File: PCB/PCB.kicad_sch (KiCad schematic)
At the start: 16 parts, among them J1 Screw_Terminal_01x02, J2 Screw_Terminal_01x02, U1 MPU-6050, U2 DRV8833PWP, U3 ESP32-S3-MINI-1

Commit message: PCB work, finished schematic Rev A
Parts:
- added C10, C11, C12, C13, C14, C9: 10uF, symbol Device:C
- added C15: 1uF, symbol Device:C
- added C16, C7: 1uF 50V, symbol Device:C
- added C8: 10uF 25V, symbol Device:C
- added D1: 1N5819, Diode_THT:D_DO-41_SOD81_P10.16mm_Horizontal, symbol Diode:1N5819
- added D2: LED, symbol Device:LED
- added J3: USB_C_Receptacle_USB2.0_14P, symbol Connector:USB_C_Receptacle_USB2.0_14P
- added R10, R6, R7, R8: 5.1K, symbol Device:R
- added R9: 100K, symbol Device:R
- added SW1, SW2: SW_Push, symbol Switch:SW_Push
- added U4: AP2112K-3.3, Package_TO_SOT_SMD:SOT-23-5, symbol Regulator_Linear:AP2112K-3.3
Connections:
- net +3.3V: now also U3.3 (3V3), C10.1, C11.1, C12.1, C13.1, C14.1, C15.1, R10.1, R6.1, U4.5 (VOUT)
- net +5V: now also C8.1, C9.1, D1.1 (K), R9.2, U4.1 (VIN)
- net AIN1: now also U3.21 (IO17)
- net AIN2: now also U3.9 (IO5)
- net BIN1: now also U3.22 (IO18)
- net BIN2: now also U3.10 (IO6)
- net GND: now also U3.1 (GND), U3.2 (GND), U3.42 (GND), U3.43 (GND), U3.46 (GND), U3.47 (GND), U3.48 (GND), U3.49 (GND), U3.50 (GND), U3.51 (GND), U3.52 (GND), U3.53 (GND), U3.54 (GND), U3.55 (GND), U3.56 (GND), U3.57 (GND), U3.58 (GND), U3.59 (GND), U3.60 (GND), U3.61 (GND), U3.62 (GND), U3.63 (GND), U3.64 (GND), U3.65 (GND), C10.2, C11.2, C12.2, C13.2, C14.2, C15.2, C16.2, C7.2, C8.2, C9.2, D2.1 (K), J3.A1 (GND), J3.A12 (GND), J3.B1 (GND), J3.B12 (GND), J3.S1 (SHIELD), R7.2, R8.2, SW1.2, SW2.1, U4.2 (GND)
- net SCL: now also U3.8 (IO4)
- net IO7: now reaches U3.11 (IO7)
- net IO8: now reaches U3.12 (IO8)
- net IO9: now reaches U3.13 (IO9)
- net IO10: now reaches U3.14 (IO10)
- net IO11: now reaches U3.15 (IO11)
- net IO12: now reaches U3.16 (IO12)
- net IO13: now reaches U3.17 (IO13)
- net IO14: now reaches U3.18 (IO14)
- net IO15: now reaches U3.19 (IO15)
- net IO16: now reaches U3.20 (IO16)
- net D-: now reaches U3.23 (IO19)
- net D-: now also J3.A7 (D-), J3.B7 (D-)
- net D+: now reaches U3.24 (IO20)
- net D+: now also J3.A6 (D+), J3.B6 (D+)
- net IO21: now reaches U3.25 (IO21)
- net IO26: now reaches U3.26 (IO26)
- net IO47: now reaches U3.27 (IO47)
- net IO33: now reaches U3.28 (IO33)
- net IO34: now reaches U3.29 (IO34)
- net IO48: now reaches U3.30 (IO48)
- net IO35: now reaches U3.31 (IO35)
- net IO36: now reaches U3.32 (IO36)
- net IO37: now reaches U3.33 (IO37)
- net IO38: now reaches U3.34 (IO38)
- net IO39: now reaches U3.35 (IO39)
- net IO40: now reaches U3.36 (IO40)
- net IO41: now reaches U3.37 (IO41)
- net IO42: now reaches U3.38 (IO42)
- net TXD0: now reaches U3.39 (TXD0)
- net BOOT0: now reaches U3.4 (IO0)
- net BOOT0: now also C16.1, SW2.2
- net RXD0: now reaches U3.40 (RXD0)
- net IO45: now reaches U3.41 (IO45)
- net IO46: now reaches U3.44 (IO46)
- net RESET: now reaches U3.45 (EN)
- net RESET: now also C7.1, R6.2, SW1.1
- net IO1: now reaches U3.5 (IO1)
- net IO2: now reaches U3.6 (IO2)
- net IO3: now reaches U3.7 (IO3)
- net INT: now reaches U1.12 (INT)
- net XDA: now reaches U1.6 (AUX_DA)
- net XCL: now reaches U1.7 (AUX_CL)
- net FAULT: now reaches U2.8 (~{FAULT})
- new net: D1.2 (A), J3.A4 (VBUS), J3.A9 (VBUS), J3.B4 (VBUS), J3.B9 (VBUS)
- new net: D2.2 (A), R10.2
- new net: J3.A5 (CC1), R8.1
- new net: J3.B5 (CC2), R7.1
- new net: R9.1, U4.3 (EN)
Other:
- note added: "ESP32"
- moved on the sheet: U3

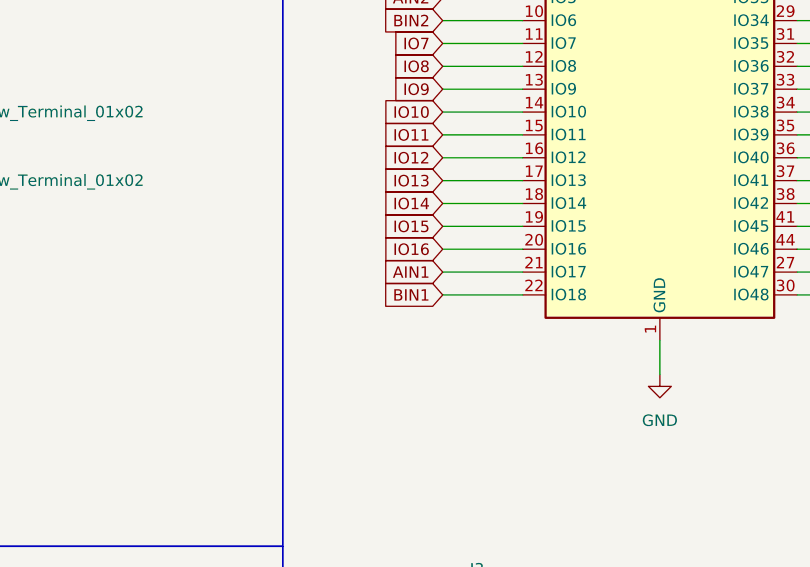
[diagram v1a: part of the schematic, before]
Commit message: Added footprints and nets to PCB file, set up design rules
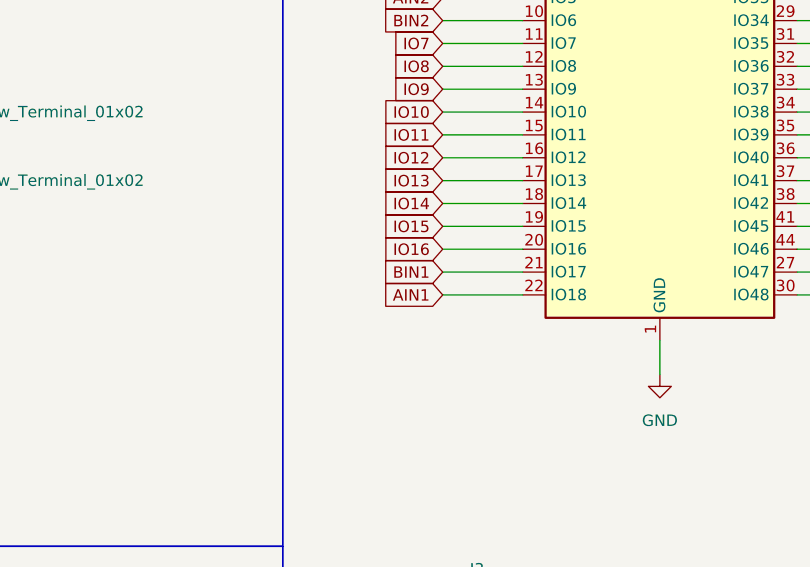
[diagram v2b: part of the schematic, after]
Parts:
- C1, C10, C11, C12, C13, C14, C15, C16, C2, C3, C4, C5, C6, C7, C8, C9: footprint (none) -> Capacitor_SMD:C_0805_2012Metric
- D2: footprint (none) -> LED_SMD:LED_0805_2012Metric
- J1, J2: footprint (none) -> Connector_Phoenix_GMSTB:PhoenixContact_GMSTBA_2,5_2-G_1x02_P7.50mm_Horizontal
- R1, R10, R2, R3, R4, R5, R6, R7, R8, R9: footprint (none) -> Resistor_SMD:R_0805_2012Metric
- SW1, SW2: footprint (none) -> Button_Switch_SMD:SW_SPST_EVPBF
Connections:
- net AIN1: now also U3.22 (IO18); no longer U3.21 (IO17)
- net BIN1: now also U3.21 (IO17); no longer U3.22 (IO18)
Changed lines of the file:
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@@
 	(wire
 		(pts
-			(xy 163.83 85.09) (xy 172.72 85.09)
-		)
-		(stroke
-			(width 0)
-			(type default)
-		)
-	)
-	(wire
-		(pts
 			(xy 203.2 57.15) (xy 210.82 57.15)
 		)
@@
 	(wire
 		(pts
-			(xy 163.83 87.63) (xy 172.72 87.63)
-		)
-		(stroke
-			(width 0)
-			(type default)
-		)
-	)
-	(wire
-		(pts
 			(xy 163.83 72.39) (xy 172.72 72.39)
 		)
@@
 	(wire
 		(pts
+			(xy 163.83 85.09) (xy 172.72 85.09)
+		)
+		(stroke
+			(width 0)
+			(type default)
+		)
+	)
+	(wire
+		(pts
 			(xy 163.83 46.99) (xy 172.72 46.99)
 		)
@@
 	(wire
 		(pts
+			(xy 163.83 87.63) (xy 172.72 87.63)
+		)
+		(stroke
+			(width 0)
+			(type default)
+		)
+	)
+	(wire
+		(pts
 			(xy 120.65 187.96) (xy 120.65 165.1)
 		)
@@
 	(global_label "BIN1"
 		(shape input)
-		(at 163.83 87.63 180)
+		(at 163.83 85.09 180)
 		(fields_autoplaced yes)
 		(effects
@@
 		)
 		(property "Intersheetrefs" "${INTERSHEET_REFS}"
-			(at 156.43 87.63 0)
+			(at 156.43 85.09 0)
 			(effects
 				(font
@@
 	(global_label "AIN1"
 		(shape input)
-		(at 163.83 85.09 180)
+		(at 163.83 87.63 180)
 		(fields_autoplaced yes)
 		(effects
@@
 		)
 		(property "Intersheetrefs" "${INTERSHEET_REFS}"
-			(at 156.6114 85.09 0)
+			(at 156.6114 87.63 0)
 			(effects
 				(font
@@
 			)
 		)
-		(property "Footprint" ""
+		(property "Footprint" "Resistor_SMD:R_0805_2012Metric"
 			(at 23.622 138.43 90)
 			(effects
@@
 			)
 		)
-		(property "Footprint" ""
+		(property "Footprint" "Resistor_SMD:R_0805_2012Metric"
 			(at 33.782 66.04 90)
 			(effects
@@
 			)
 		)
-		(property "Footprint" ""
+		(property "Footprint" "Connector_Phoenix_GMSTB:PhoenixContact_GMSTBA_2,5_2-G_1x02_P7.50mm_Horizontal"
 			(at 107.95 72.39 0)
 			(effects
@@
 			)
 		)
-		(property "Footprint" ""
+		(property "Footprint" "Capacitor_SMD:C_0805_2012Metric"
 			(at 352.7552 99.06 0)
 			(effects
@@
 			)
 		)
-		(property "Footprint" ""
+		(property "Footprint" "Capacitor_SMD:C_0805_2012Metric"
 			(at 122.8852 137.16 0)
 			(effects
@@
 			)
 		)
-		(property "Footprint" ""
+		(property "Footprint" "LED_SMD:LED_0805_2012Metric"
 			(at 382.27 95.25 0)
 			(effects
@@
 			)
 		)
-		(property "Footprint" ""
+		(property "Footprint" "Resistor_SMD:R_0805_2012Metric"
 			(at 268.732 135.89 90)
 			(effects
@@
 			)
 		)
-		(property "Footprint" ""
+		(property "Footprint" "Resistor_SMD:R_0805_2012Metric"
 			(at 46.482 167.64 90)
 			(effects
@@
 			)
 		)
-		(property "Footprint" ""
+		(property "Footprint" "Resistor_SMD:R_0805_2012Metric"
 			(at 210.312 139.7 90)
 			(effects
@@
 			)
 		)
-		(property "Footprint" ""
+		(property "Footprint" "Capacitor_SMD:C_0805_2012Metric"
 			(at 224.4852 143.51 0)
 			(effects
@@
 			)
 		)
-		(property "Footprint" ""
+		(property "Footprint" "Resistor_SMD:R_0805_2012Metric"
 			(at 200.152 139.7 90)
 			(effects
@@
 			)
 		)
-		(property "Footprint" ""
+		(property "Footprint" "Capacitor_SMD:C_0805_2012Metric"
 			(at 74.93 139.3952 0)
 			(effects
@@
 			)
 		)
-		(property "Footprint" ""
+		(property "Footprint" "Resistor_SMD:R_0805_2012Metric"
 			(at 43.942 66.04 90)
 			(effects
@@
 			)
 		)
-		(property "Footprint" ""
+		(property "Footprint" "Capacitor_SMD:C_0805_2012Metric"
 			(at 324.8152 99.06 0)
 			(effects
@@
 			)
 		)
-		(property "Footprint" ""
+		(property "Footprint" "Button_Switch_SMD:SW_SPST_EVPBF"
 			(at 350.52 137.16 0)
 			(effects
@@
 			)
 		)
-		(property "Footprint" ""
+		(property "Footprint" "Resistor_SMD:R_0805_2012Metric"
 			(at 374.65 90.678 90)
 			(effects
@@
 			)
 		)
-		(property "Footprint" ""
+		(property "Footprint" "Capacitor_SMD:C_0805_2012Metric"
 			(at 338.7852 99.06 0)
 			(effects
@@
 			)
 		)
-		(property "Footprint" ""
+		(property "Footprint" "Capacitor_SMD:C_0805_2012Metric"
 			(at 53.0352 53.34 0)
 			(effects
@@
 			)
 		)
-		(property "Footprint" ""
+		(property "Footprint" "Capacitor_SMD:C_0805_2012Metric"
 			(at 80.01 188.9252 0)
 			(effects
@@
 			)
 		)
-		(property "Footprint" ""
+		(property "Footprint" "Connector_Phoenix_GMSTB:PhoenixContact_GMSTBA_2,5_2-G_1x02_P7.50mm_Horizontal"
 			(at 107.95 64.77 0)
 			(effects
@@
 			)
 		)
-		(property "Footprint" ""
+		(property "Footprint" "Capacitor_SMD:C_0805_2012Metric"
 			(at 366.7252 99.06 0)
 			(effects
@@
 			)
 		)
-		(property "Footprint" ""
+		(property "Footprint" "Capacitor_SMD:C_0805_2012Metric"
 			(at 287.9852 156.21 0)
 			(effects
@@
 			)
 		)
-		(property "Footprint" ""
+		(property "Footprint" "Button_Switch_SMD:SW_SPST_EVPBF"
 			(at 275.59 152.4 0)
 			(effects
@@
 			)
 		)
-		(property "Footprint" ""
+		(property "Footprint" "Resistor_SMD:R_0805_2012Metric"
 			(at 267.97 94.742 90)
 			(effects
@@
 			)
 		)
-		(property "Footprint" ""
+		(property "Footprint" "Capacitor_SMD:C_0805_2012Metric"
 			(at 254.9652 101.6 0)
 			(effects
@@
 			)
 		)
-		(property "Footprint" ""
+		(property "Footprint" "Capacitor_SMD:C_0805_2012Metric"
 			(at 131.7752 171.45 0)
 			(effects
@@
 			)
 		)
-		(property "Footprint" ""
+		(property "Footprint" "Resistor_SMD:R_0805_2012Metric"
 			(at 46.482 138.43 90)
 			(effects
@@
 			)
 		)
-		(property "Footprint" ""
+		(property "Footprint" "Capacitor_SMD:C_0805_2012Metric"
 			(at 359.1052 154.94 0)
 			(effects
@@
 			)
 		)
-		(property "Footprint" ""
+		(property "Footprint" "Capacitor_SMD:C_0805_2012Metric"
 			(at 310.8452 99.06 0)
 			(effects
@@
 			)
 		)
-		(property "Footprint" ""
+		(property "Footprint" "Capacitor_SMD:C_0805_2012Metric"
 			(at 296.8752 99.06 0)
 			(effects
@@
 			)
 		)
-		(property "Footprint" ""
+		(property "Footprint" "Capacitor_SMD:C_0805_2012Metric"
 			(at 86.36 39.0652 0)
 			(effects

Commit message: PCB Progress
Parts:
- removed J3: USB_C_Receptacle_USB2.0_14P, symbol Connector:USB_C_Receptacle_USB2.0_14P
- added J3: USB_C_Receptacle_USB2.0_16P, Connector_USB:USB_C_Receptacle_G-Switch_GT-USB-7010ASV, symbol Connector:USB_C_Receptacle_USB2.0_16P
- J1: footprint Connector_Phoenix_GMSTB:PhoenixContact_GMSTBA_2,5_2-G_1x02_P7.50mm_Horizontal -> Connector_PinSocket_2.54mm:PinSocket_1x02_P2.54mm_Vertical
- J2: footprint Connector_Phoenix_GMSTB:PhoenixContact_GMSTBA_2,5_2-G_1x02_P7.50mm_Horizontal -> Connector_PinHeader_2.54mm:PinHeader_1x02_P2.54mm_Vertical
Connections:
- net D+: now also J3.A6 (D+), J3.B6 (D+)
- net D-: now also J3.A7 (D-), J3.B7 (D-)
- net GND: now also J3.A1 (GND), J3.A12 (GND), J3.B1 (GND), J3.B12 (GND), J3.S1 (SHIELD)
- net at D1.2 (A): now also J3.A4 (VBUS), J3.A9 (VBUS), J3.B4 (VBUS), J3.B9 (VBUS)
- net at R8.1: now also J3.A5 (CC1)
- net at R7.1: now also J3.B5 (CC2)
- new net SBU1: J3.A8 (SBU1)
- new net SBU2: J3.B8 (SBU2)
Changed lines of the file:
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@@
 		)
 	)
+	(global_label "SBU2"
+		(shape input)
+		(at 182.88 156.21 0)
+		(fields_autoplaced yes)
+		(effects
+			(font
+				(size 1.27 1.27)
+			)
+			(justify left)
+		)
+		(property "Intersheetrefs" "${INTERSHEET_REFS}"
+			(at 190.8847 156.21 0)
+			(effects
+				(font
+					(size 1.27 1.27)
+				)
+				(justify left)
+				(hide yes)
+			)
+		)
+	)
 	(global_label "IO46"
 		(shape input)
@@
 		)
 	)
+	(global_label "SBU1"
+		(shape input)
+		(at 182.88 153.67 0)
+		(fields_autoplaced yes)
+		(effects
+			(font
+				(size 1.27 1.27)
+			)
+			(justify left)
+		)
+		(property "Intersheetrefs" "${INTERSHEET_REFS}"
+			(at 190.8847 153.67 0)
+			(effects
+				(font
+					(size 1.27 1.27)
+				)
+				(justify left)
+				(hide yes)
+			)
+		)
+	)
 	(global_label "IO33"
 		(shape input)
@@
 			)
 		)
-		(property "Footprint" "Connector_Phoenix_GMSTB:PhoenixContact_GMSTBA_2,5_2-G_1x02_P7.50mm_Horizontal"
+		(property "Footprint" "Connector_PinHeader_2.54mm:PinHeader_1x02_P2.54mm_Vertical"
 			(at 107.95 72.39 0)
 			(effects
@@
 			)
 		)
-		(property "Footprint" "Connector_Phoenix_GMSTB:PhoenixContact_GMSTBA_2,5_2-G_1x02_P7.50mm_Horizontal"
+		(property "Footprint" "Connector_PinSocket_2.54mm:PinSocket_1x02_P2.54mm_Vertical"
 			(at 107.95 64.77 0)
 			(effects
@@
 	)
 	(symbol
+		(lib_id "Connector:USB_C_Receptacle_USB2.0_16P")
+		(at 167.64 140.97 0)
+		(unit 1)
+		(exclude_from_sim no)
+		(in_bom yes)
+		(on_board yes)
+		(dnp no)
+		(fields_autoplaced yes)
+		(property "Reference" "J3"
+			(at 167.64 118.11 0)
+			(effects
+				(font
+					(size 1.27 1.27)
+				)
+			)
+		)
+		(property "Value" "USB_C_Receptacle_USB2.0_16P"
+			(at 167.64 120.65 0)
+			(effects
+				(font
+					(size 1.27 1.27)
+				)
+			)
+		)
+		(property "Footprint" "Connector_USB:USB_C_Receptacle_G-Switch_GT-USB-7010ASV"
+			(at 171.45 140.97 0)
+			(effects
+				(font
+					(size 1.27 1.27)
+				)
+				(hide yes)
+			)
+		)
+		(property "Datasheet" "https://www.usb.org/sites/default/files/documents/usb_type-c.zip"
+			(at 171.45 140.97 0)
+			(effects
+				(font
+					(size 1.27 1.27)
+				)
+				(hide yes)
+			)
+		)
+		(property "Description" "USB 2.0-only 16P Type-C Receptacle connector"
+			(at 167.64 140.97 0)
+			(effects
+				(font
+					(size 1.27 1.27)
+				)
+				(hide yes)
+			)
+		)
+		(pin "A1"
+		)
+		(pin "B4"
+		)
+		(pin "A8"
+		)
+		(pin "A4"
+		)
+		(pin "A9"
+		)
+		(pin "A12"
+		)
+		(pin "B6"
+		)
+		(pin "B7"
+		)
+		(pin "B5"
+		)
+		(pin "A6"
+		)
+		(pin "S1"
+		)
+		(pin "A5"
+		)
+		(pin "A7"
+		)
+		(pin "B1"
+		)
+		(pin "B12"
+		)
+		(pin "B8"
+		)
+		(pin "B9"
+		)
+		(instances
+			(project ""
+				(path "/1d0c519c-16f4-4a16-b94e-0bddce7294e9"
+					(reference "J3")
+					(unit 1)
+				)
+			)
+		)
+	)
+	(symbol
 		(lib_id "Switch:SW_Push")
 		(at 270.51 152.4 270)
@@
 					(unit 1)
 				)
-			)
-		)
-	)
-	(symbol
-		(lib_id "Connector:USB_C_Receptacle_USB2.0_14P")
-		(at 167.64 140.97 0)
-		(unit 1)
-		(exclude_from_sim no)
-		(in_bom yes)
-		(on_board yes)
-		(dnp no)
-		(fields_autoplaced yes)
-		(property "Reference" "J3"
-			(at 167.64 118.11 0)
-			(effects
-				(font
-					(size 1.27 1.27)
-				)
-			)
-		)
-		(property "Value" "USB_C_Receptacle_USB2.0_14P"
-			(at 167.64 120.65 0)
-			(effects
-				(font
-					(size 1.27 1.27)
-				)
-			)
-		)
-		(property "Footprint" ""
-			(at 171.45 140.97 0)
-			(effects
-				(font
-					(size 1.27 1.27)
-				)
-				(hide yes)
-			)
-		)
-		(property "Datasheet" "https://www.usb.org/sites/default/files/documents/usb_type-c.zip"
-			(at 171.45 140.97 0)
-			(effects
-				(font
-					(size 1.27 1.27)
-				)
-				(hide yes)
-			)
-		)
-		(property "Description" "USB 2.0-only 14P Type-C Receptacle connector"
-			(at 167.64 140.97 0)
-			(effects
-				(font
-					(size 1.27 1.27)
-				)
-				(hide yes)
-			)
-		)
-		(pin "A1"
-		)
-		(pin "A5"
-		)
-		(pin "A7"
-		)
-		(pin "A9"
-		)
-		(pin "B1"
-		)
-		(pin "A4"
-		)
-		(pin "A6"
-		)
-		(pin "A12"
-		)
-		(pin "B7"
-		)
-		(pin "B4"
-		)
-		(pin "B12"
-		)
-		(pin "B5"
-		)
-		(pin "B9"
-		)
-		(pin "S1"
-		)
-		(pin "B6"
-		)
-		(instances
-			(project ""
-				(path "/1d0c519c-16f4-4a16-b94e-0bddce7294e9"
-					(reference "J3")
-					(unit 1)
-				)

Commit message: Finished second PCB
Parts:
- removed J3: USB_C_Receptacle_USB2.0_16P, Connector_USB:USB_C_Receptacle_G-Switch_GT-USB-7010ASV, symbol Connector:USB_C_Receptacle_USB2.0_16P
- added J3: USB_C_Receptacle, Connector_USB:USB_C_Receptacle_Amphenol_12401610E4-2A, symbol Connector:USB_C_Receptacle
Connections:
- net D+: now also J3.A6 (D+), J3.B6 (D+)
- net D-: now also J3.A7 (D-), J3.B7 (D-)
- net GND: now also J3.A1 (GND), J3.A12 (GND), J3.B1 (GND), J3.B12 (GND), J3.S1 (SHIELD)
- net SBU1: now also J3.A8 (SBU1)
- net SBU2: now also J3.B8 (SBU2)
- net at D1.2 (A): now also J3.A4 (VBUS), J3.A9 (VBUS), J3.B4 (VBUS), J3.B9 (VBUS)
- net at R8.1: now also J3.A5 (CC1)
- net at R7.1: now also J3.B5 (CC2)
- new net RX1+: J3.B11 (RX1+)
- new net RX1-: J3.B10 (RX1-)
- new net RX2+: J3.A11 (RX2+)
- new net RX2-: J3.A10 (RX2-)
- new net TX1+: J3.A2 (TX1+)
- new net TX1-: J3.A3 (TX1-)
- new net TX2+: J3.B2 (TX2+)
- new net TX2-: J3.B3 (TX2-)
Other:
- moved on the sheet: C8, D1, R7, R8
